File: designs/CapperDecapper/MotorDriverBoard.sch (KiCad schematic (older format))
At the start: 17 parts, among them J1 Conn_01x20, U1 DRV8837DSGR, U2 DRV8837DSGR, U3 DRV8837DSGR, U4 DRV8837DSGR, U5 DRV8837DSGR, U6 DRV8837DSGR, U7 DRV8837DSGR, U8 DRV8837DSGR

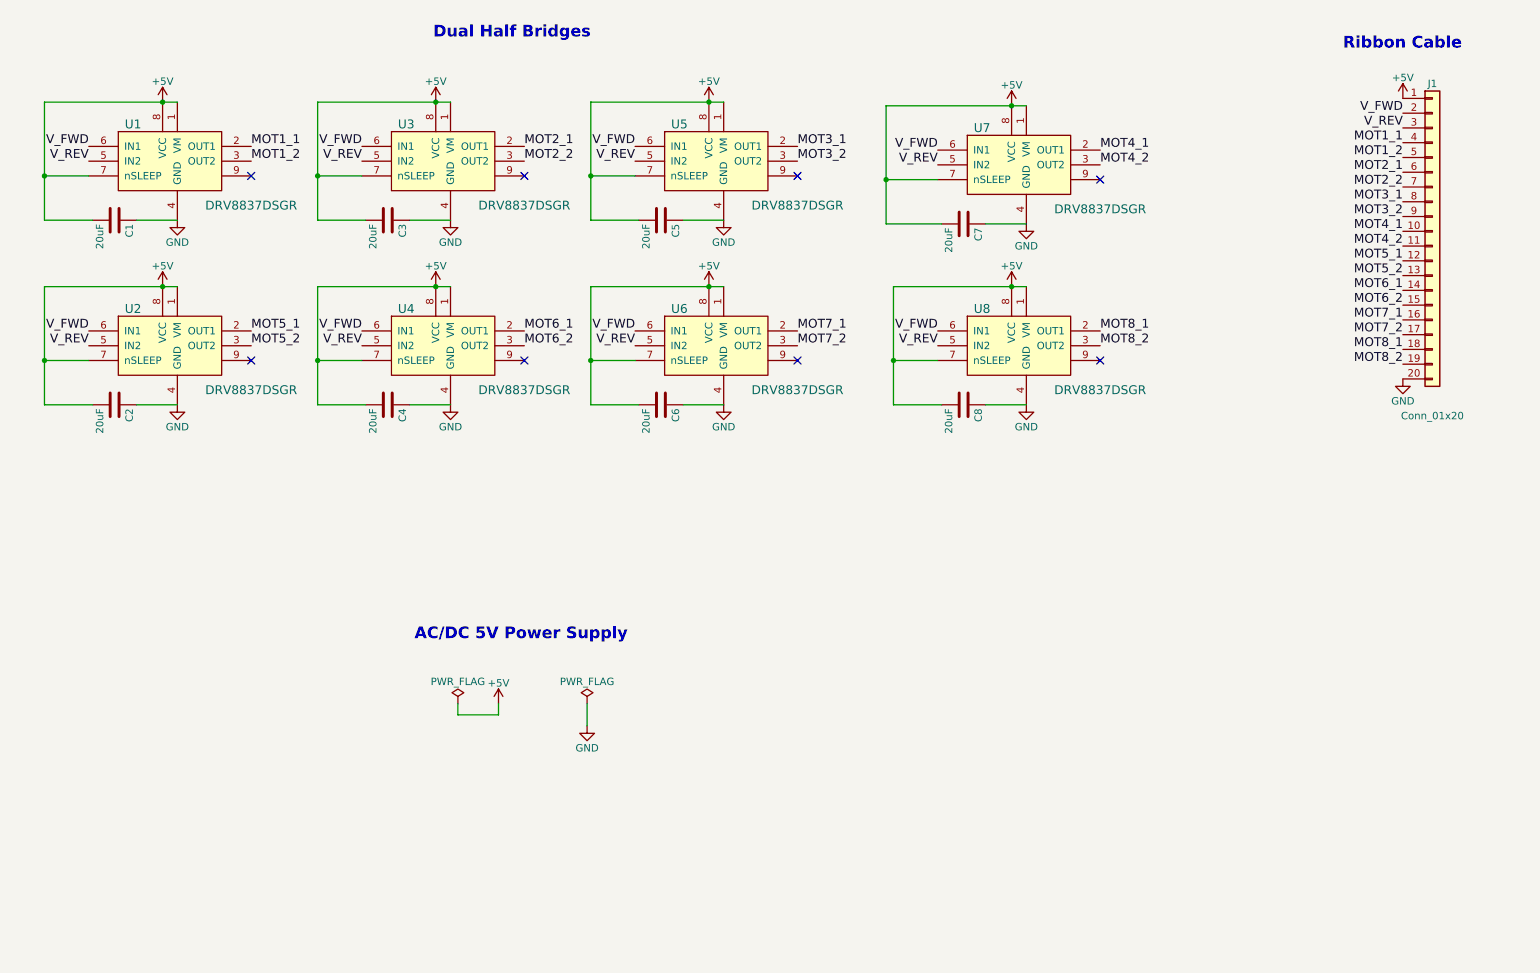
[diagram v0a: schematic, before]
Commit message: Capper Decapper added with custom components
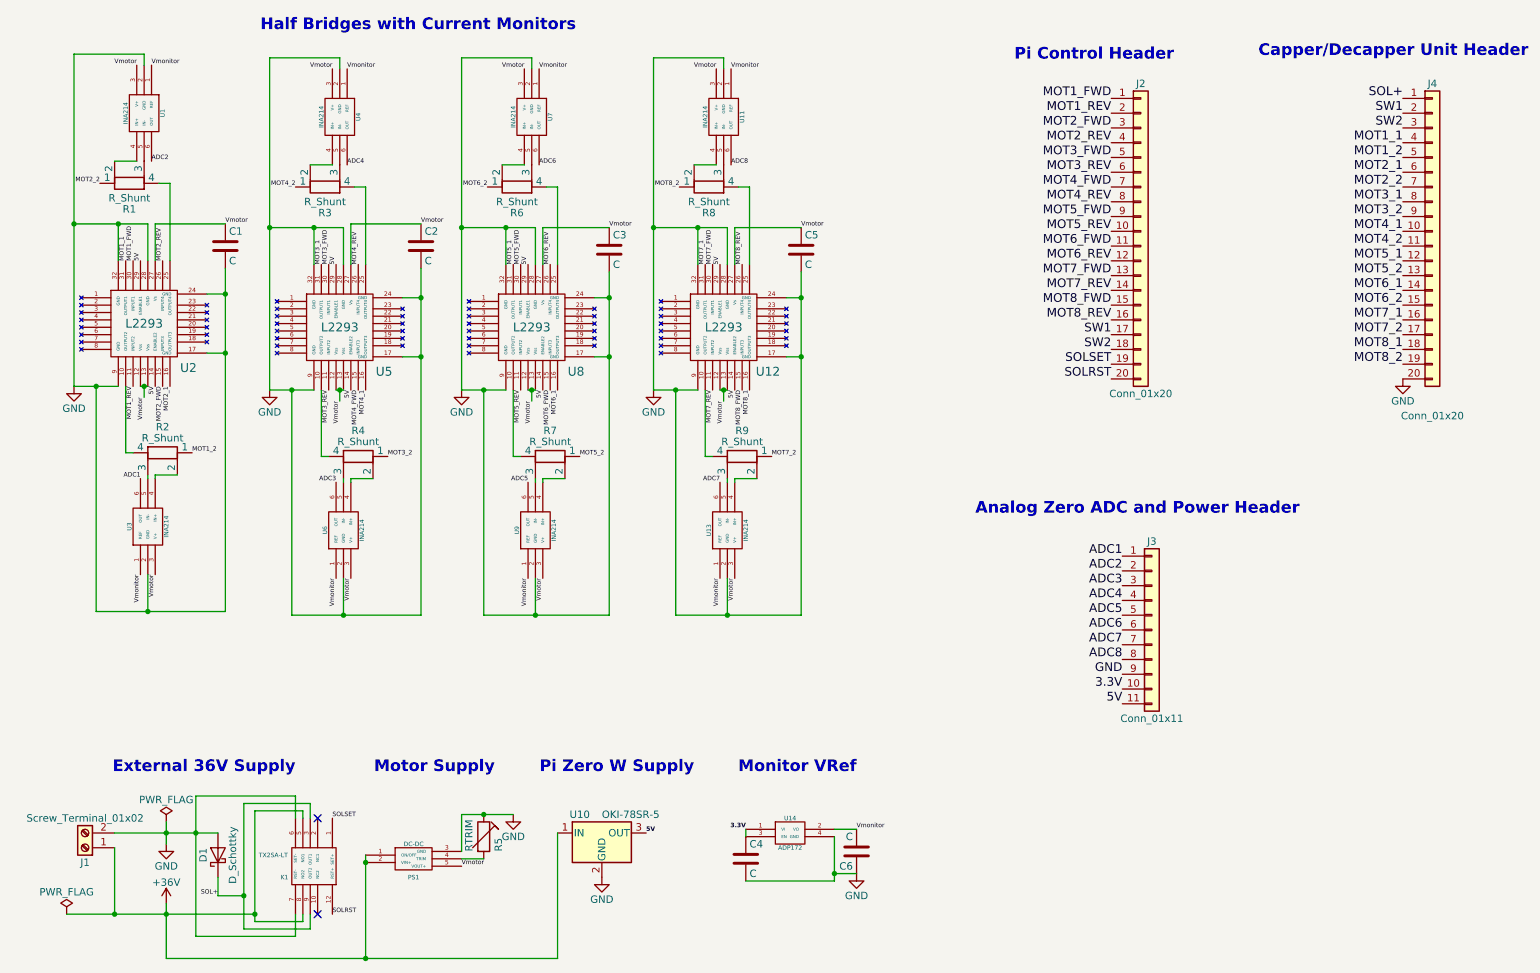
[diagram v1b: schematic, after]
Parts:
- removed C7, C8: 20uF, symbol C
- removed U1, U2, U3, U4, U5, U6, U7, U8: DRV8837DSGR, digikey-footprints:WSON-8_2x2mm, symbol DRV8837DSGR
- added D1: D_Schottky, symbol D_Schottky
- added J1: Screw_Terminal_01x02, Connectors_Terminal_Blocks:TerminalBlock_Pheonix_PT-3.5mm_2pol, symbol Screw_Terminal_01x02
- added J2: Conn_01x20, symbol Conn_01x20
- added J3: Conn_01x11, symbol Conn_01x11
- added K1: TX2SA-LT, symbol TX2SA-LT
- added PS1: DC-DC, symbol DC-DC
- added R1, R2, R3, R4, R6, R7, R8, R9: R_Shunt, Resistors_SMD:R_Array_Convex_2x1206, symbol R_Shunt
- added R5: RTRIM, symbol RTRIM
- added U1, U11, U13, U3, U4, U6, U7, U9: INA214, TO_SOT_Packages_SMD:SOT-363_SC-70-6, symbol INA214
- added U10: OKI-78SR-5, symbol L7805
- added U12, U2, U5, U8: L2293, Housings_DFN_QFN:WQFN-32-1EP_5x5mm_Pitch0.5mm, symbol L2293
- added U14: ADP172, symbol ADP172
- C1, C2, C3, C4, C5, C6: value 20uF -> C; footprint (none) -> Capacitors_SMD:C_0603
- renumbered J1 to J4
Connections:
- net GND: now also C1.2, C2.2, C3.2, C4.2, C5.2, D1.2 (A), J1.2 (Pin_2), J3.9 (Pin_9), K1.6 (SET-), K1.7 (RST-), PS1.3 (GND), R5.1, U1.2 (GND), U10.2 (GND), U11.2 (GND), U12.17 (GND), U12.24 (GND), U12.28 (GND), U12.32 (GND), U12.9 (GND), U13.2 (GND), U14.4 (GND), U2.17 (GND), U2.24 (GND), U2.28 (GND), U2.32 (GND), U2.9 (GND), U3.2 (GND), U4.2 (GND), U5.17 (GND), U5.24 (GND), U5.28 (GND), U5.32 (GND), U5.9 (GND), U6.2 (GND), U7.2 (GND), U8.17 (GND), U8.24 (GND), U8.28 (GND), U8.32 (GND), U8.9 (GND), U9.2 (GND); no longer C1.1, C2.1, C3.1, C4.1, C5.1
- net MOT1_1: now also U2.31 (OUTPUT1)
- net MOT1_2: now also R2.1
- net MOT2_1: now also U2.16 (OUTPUT3)
- net MOT2_2: now also R1.1
- net MOT3_1: now also U5.31 (OUTPUT1)
- net MOT3_2: now also R4.1
- net MOT4_1: now also U5.16 (OUTPUT3)
- net MOT4_2: now also R3.1
- net MOT5_1: now also U8.31 (OUTPUT1)
- net MOT5_2: now also R7.1
- net MOT6_1: now also U8.16 (OUTPUT3)
- net MOT6_2: now also R6.1
- net MOT7_1: now also U12.31 (OUTPUT1)
- net MOT7_2: now also R9.1
- net MOT8_1: now also U12.16 (OUTPUT3)
- net MOT8_2: now also R8.1
- removed net +5V: C1.2, C2.2, C3.2, C4.2, C5.2, C6.2, J4.1 (Pin_1)
- net V_FWD renamed SW1
- net SW1: now also J2.17 (Pin_17)
- net V_REV renamed SW2
- net SW2: now also J2.18 (Pin_18)
- new net: R2.4, U2.10 (OUTPUT2)
- new net: R1.4, U2.25 (OUTPUT4)
- new net: R2.2, U3.4 (IN+)
- new net: R2.3, U3.5 (IN-)
- new net: R1.2, U1.4 (IN+)
- new net: R1.3, U1.5 (IN-)
- new net: R4.4, U5.10 (OUTPUT2)
- new net: R3.4, U5.25 (OUTPUT4)
- new net: R4.2, U6.4 (IN+)
- new net: R4.3, U6.5 (IN-)
- new net: R3.2, U4.4 (IN+)
- new net: R3.3, U4.5 (IN-)
- new net: R7.4, U8.10 (OUTPUT2)
- new net: R6.4, U8.25 (OUTPUT4)
- new net: R7.2, U9.4 (IN+)
- new net: R7.3, U9.5 (IN-)
- new net: R6.2, U7.4 (IN+)
- new net: R6.3, U7.5 (IN-)
- new net: R9.4, U12.10 (OUTPUT2)
- new net: R8.4, U12.25 (OUTPUT4)
- new net: R9.2, U13.4 (IN+)
- new net: R9.3, U13.5 (IN-)
- new net: R8.2, U11.4 (IN+)
- new net: R8.3, U11.5 (IN-)
- new net: PS1.4 (TRIM), R5.2
- new net +36V: J1.1 (Pin_1), K1.5 (NO1), K1.8 (NO2), PS1.1 (ON/OFF), PS1.2 (VIN+), U10.1 (IN)
- new net 3.3V: C4.1, J3.10 (Pin_10), U14.1 (VI), U14.3 (EN)
- new net 5V: J3.11 (Pin_11), U10.3 (OUT), U12.14 (ENABLE2), U12.29 (ENABLE1), U2.14 (ENABLE2), U2.29 (ENABLE1), U5.14 (ENABLE2), U5.29 (ENABLE1), U8.14 (ENABLE2), U8.29 (ENABLE1)
- new net ADC1: J3.1 (Pin_1), U3.6 (OUT)
- new net ADC2: J3.2 (Pin_2), U1.6 (OUT)
- new net ADC3: J3.3 (Pin_3), U6.6 (OUT)
- new net ADC4: J3.4 (Pin_4), U4.6 (OUT)
- new net ADC5: J3.5 (Pin_5), U9.6 (OUT)
- new net ADC6: J3.6 (Pin_6), U7.6 (OUT)
- new net ADC7: J3.7 (Pin_7), U13.6 (OUT)
- new net ADC8: J3.8 (Pin_8), U11.6 (OUT)
- new net MOT1_FWD: J2.1 (Pin_1), U2.30 (INPUT1)
- new net MOT1_REV: J2.2 (Pin_2), U2.11 (INPUT2)
- new net MOT2_FWD: J2.3 (Pin_3), U2.15 (INPUT3)
- new net MOT2_REV: J2.4 (Pin_4), U2.26 (INPUT4)
- new net MOT3_FWD: J2.5 (Pin_5), U5.30 (INPUT1)
- new net MOT3_REV: J2.6 (Pin_6), U5.11 (INPUT2)
- new net MOT4_FWD: J2.7 (Pin_7), U5.15 (INPUT3)
- new net MOT4_REV: J2.8 (Pin_8), U5.26 (INPUT4)
- new net MOT5_FWD: J2.9 (Pin_9), U8.30 (INPUT1)
- new net MOT5_REV: J2.10 (Pin_10), U8.11 (INPUT2)
- new net MOT6_FWD: J2.11 (Pin_11), U8.15 (INPUT3)
- new net MOT6_REV: J2.12 (Pin_12), U8.26 (INPUT4)
- new net MOT7_FWD: J2.13 (Pin_13), U12.30 (INPUT1)
- new net MOT7_REV: J2.14 (Pin_14), U12.11 (INPUT2)
- new net MOT8_FWD: J2.15 (Pin_15), U12.15 (INPUT3)
- new net MOT8_REV: J2.16 (Pin_16), U12.26 (INPUT4)
- new net SOL+: D1.1 (K), J4.1 (Pin_1), K1.3 (OUT1), K1.9 (OUT2)
- new net SOLRST: J2.20 (Pin_20), K1.12 (RST+)
- new net SOLSET: J2.19 (Pin_19), K1.1 (SET+)
- new net Vmonitor: C6.2, U1.1 (REF), U11.1 (REF), U13.1 (REF), U14.2 (VO), U3.1 (REF), U4.1 (REF), U6.1 (REF), U7.1 (REF), U9.1 (REF)
- new net Vmotor: C1.1, C2.1, C3.1, C5.1, PS1.5 (VOUT+), U1.3 (V+), U11.3 (V+), U12.12 (Vss), U12.13 (Vss), U12.27 (Vs), U13.3 (V+), U2.12 (Vss), U2.13 (Vss), U2.27 (Vs), U3.3 (V+), U4.3 (V+), U5.12 (Vss), U5.13 (Vss), U5.27 (Vs), U6.3 (V+), U7.3 (V+), U8.12 (Vss), U8.13 (Vss), U8.27 (Vs), U9.3 (V+)
- no-connect marks 8 -> 2
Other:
- note added: "Analog Zero ADC and Power Header"
- note added: "Capper/Decapper Unit Header"
- note added: "External 36V Supply"
- note added: "Half Bridges with Current Monitors"
- note added: "Monitor VRef"
- note added: "Motor Supply"
- note added: "Pi Control Header"
- note added: "Pi Zero W Supply"
- note removed: "AC/DC 5V Power Supply"
- note removed: "Dual Half Bridges"
- note removed: "Ribbon Cable"
